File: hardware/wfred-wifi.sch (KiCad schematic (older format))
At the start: 9 parts, among them K401 UART_ESP, K402 UART_AVR, P401 ESP_BOOTLOAD, U401 ESP-12E

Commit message: Removed wiFred info from from clock project
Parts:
- removed K402: UART_AVR, Pin_Headers:Pin_Header_Straight_1x03_Pitch2.54mm, symbol CONN_3
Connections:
- net labels removed: THIS_RXD, THIS_TXD
- wire segments 29 -> 25
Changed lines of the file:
@@
 EESchema Schematic File Version 2
-LIBS:wfred_rev2-rescue
 LIBS:power
 LIBS:device
@@
 LIBS:my_devices
 LIBS:ESP8266
-LIBS:LDL1117S30R
-LIBS:MCP73831T-2ACI_OT
-LIBS:NCV8161BSN300T1G
-LIBS:wfred_rev2-cache
+LIBS:wfred_loconet_clock-cache
 EELAYER 25 0
 EELAYER END
 $Descr A4 11693 8268
 encoding utf-8
-Sheet 4 4
+Sheet 2 3
 Title "Wireless FREDI (and clock interface)"
 Date "2017-11-19"
@@
 Wire Wire Line
 	6750 2500 6700 2500
-Wire Wire Line
-	7700 2300 8050 2300
-Wire Wire Line
-	7700 2400 8050 2400
-Text GLabel 8050 2300 2    60   Output ~ 0
-THIS_RXD
-Text GLabel 8050 2400 2    60   Input ~ 0
-THIS_TXD
 $Comp
 L CONN_2 P401
@@
 Wire Wire Line
 	5200 2700 6750 2700
-$Comp
-L GND-RESCUE-wfred_rev2 #PWR041
-U 1 1 5A11FC27
-P 7850 2500
-F 0 "#PWR041" H 7850 2500 30  0001 C CNN
-F 1 "GND" H 7850 2430 30  0001 C CNN
-F 2 "" H 7850 2500 60  0001 C CNN
-F 3 "" H 7850 2500 60  0001 C CNN
-	1    7850 2500
-	1    0    0    -1
-$EndComp
 $Comp
 L R-RESCUE-wfred_rev2 R403
@@
 Wire Wire Line
 	5200 2900 6100 2900
-$Comp
-L CONN_3 K402
-U 1 1 5A11F053
-P 7350 2300
-F 0 "K402" V 7300 2300 50  0000 C CNN
-F 1 "UART_AVR" V 7400 2300 40  0000 C CNN
-F 2 "Pin_Headers:Pin_Header_Straight_1x03_Pitch2.54mm" H 7350 2300 60  0001 C CNN
-F 3 "" H 7350 2300 60  0001 C CNN
-F 4 "RND 205-00631" V 7350 2300 60  0001 C CNN "Reichelt"
-	1    7350 2300
-	-1   0    0    -1
-$EndComp
-Wire Wire Line
-	7700 2200 7850 2200
-Wire Wire Line
-	7850 2200 7850 2500
 Wire Wire Line
 	6100 2200 6100 2700

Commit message: Fix schematic after untangling from wiFred
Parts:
- C401, C402: symbol C-RESCUE-wfred_rev2 -> C
- R403, R404, R405: symbol R-RESCUE-wfred_rev2 -> R
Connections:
- net labels added: CLOCK1, CLOCK2, LOCO1, LOCO2, LOCO3, LOCO4
- wire segments 25 -> 31
- no-connect marks 14 -> 8
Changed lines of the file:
@@
 NoConn ~ 4550 3500
 $Comp
-L VCC #PWR038
+L VCC #PWR011
 U 1 1 5A11E004
 P 2700 1500
-F 0 "#PWR038" H 2700 1600 30  0001 C CNN
+F 0 "#PWR011" H 2700 1600 30  0001 C CNN
 F 1 "VCC" H 2700 1600 30  0000 C CNN
 F 2 "" H 2700 1500 60  0001 C CNN
@@
 Connection ~ 2700 2500
 $Comp
-L GND-RESCUE-wfred_rev2 #PWR039
+L GND #PWR012
 U 1 1 5A11E30D
 P 6700 3700
-F 0 "#PWR039" H 6700 3700 30  0001 C CNN
+F 0 "#PWR012" H 6700 3700 30  0001 C CNN
 F 1 "GND" H 6700 3630 30  0001 C CNN
 F 2 "" H 6700 3700 60  0001 C CNN
@@
 Connection ~ 6700 3000
 $Comp
-L VCC #PWR040
+L VCC #PWR013
 U 1 1 5A11E4AA
 P 6300 1550
-F 0 "#PWR040" H 6300 1650 30  0001 C CNN
+F 0 "#PWR013" H 6300 1650 30  0001 C CNN
 F 1 "VCC" H 6300 1650 30  0000 C CNN
 F 2 "" H 6300 1550 60  0001 C CNN
@@
 	5200 2700 6750 2700
 $Comp
-L R-RESCUE-wfred_rev2 R403
+L R R403
 U 1 1 5A11FF91
 P 6100 1950
@@
 $EndComp
 $Comp
-L R-RESCUE-wfred_rev2 R404
+L R R404
 U 1 1 5A11FFE4
 P 6100 3350
@@
 $EndComp
 $Comp
-L R-RESCUE-wfred_rev2 R405
+L R R405
 U 1 1 5A120047
 P 6300 1950
@@
 	6100 2900 6100 3100
 $Comp
-L GND-RESCUE-wfred_rev2 #PWR042
+L GND #PWR014
 U 1 1 5A120E87
 P 6100 3700
-F 0 "#PWR042" H 6100 3700 30  0001 C CNN
+F 0 "#PWR014" H 6100 3700 30  0001 C CNN
 F 1 "GND" H 6100 3630 30  0001 C CNN
 F 2 "" H 6100 3700 60  0001 C CNN
@@
 Connection ~ 6700 2900
 $Comp
-L C-RESCUE-wfred_rev2 C401
+L C C401
 U 1 1 5A127BCA
 P 1200 2400
@@
 $EndComp
 $Comp
-L VCC #PWR043
+L VCC #PWR015
 U 1 1 5A127C0E
 P 1200 1800
-F 0 "#PWR043" H 1200 1900 30  0001 C CNN
+F 0 "#PWR015" H 1200 1900 30  0001 C CNN
 F 1 "VCC" H 1200 1900 30  0000 C CNN
 F 2 "" H 1200 1800 60  0001 C CNN
@@
 	1200 1800 1200 2200
 $Comp
-L GND-RESCUE-wfred_rev2 #PWR044
+L GND #PWR016
 U 1 1 5A127CDB
 P 1200 2900
-F 0 "#PWR044" H 1200 2900 30  0001 C CNN
+F 0 "#PWR016" H 1200 2900 30  0001 C CNN
 F 1 "GND" H 1200 2830 30  0001 C CNN
 F 2 "" H 1200 2900 60  0001 C CNN
@@
 	1200 2600 1200 2900
 $Comp
-L C-RESCUE-wfred_rev2 C402
+L C C402
 U 1 1 5A199174
 P 1500 2400
@@
 	1500 2800 1200 2800
 Connection ~ 1200 2800
-NoConn ~ 5200 2500
-NoConn ~ 5200 2600
-NoConn ~ 3400 2600
-NoConn ~ 3400 2700
-NoConn ~ 3400 2800
-NoConn ~ 3400 2900
 NoConn ~ 3400 2400
 NoConn ~ 3400 2300
+Text GLabel 3200 2600 0    60   Input ~ 0
+LOCO1
+Wire Wire Line
+	3200 2600 3400 2600
+Text GLabel 3200 2700 0    60   Input ~ 0
+LOCO2
+Text GLabel 3200 2800 0    60   Input ~ 0
+LOCO3
+Text GLabel 3200 2900 0    60   Input ~ 0
+LOCO4
+Wire Wire Line
+	3200 2900 3400 2900
+Wire Wire Line
+	3400 2800 3200 2800
+Wire Wire Line
+	3200 2700 3400 2700
+Text GLabel 5500 2500 2    60   Output ~ 0
+CLOCK1
+Text GLabel 5500 2600 2    60   Output ~ 0
+CLOCK2
+Wire Wire Line
+	5200 2500 5500 2500
+Wire Wire Line
+	5500 2600 5200 2600
 $EndSCHEMATC

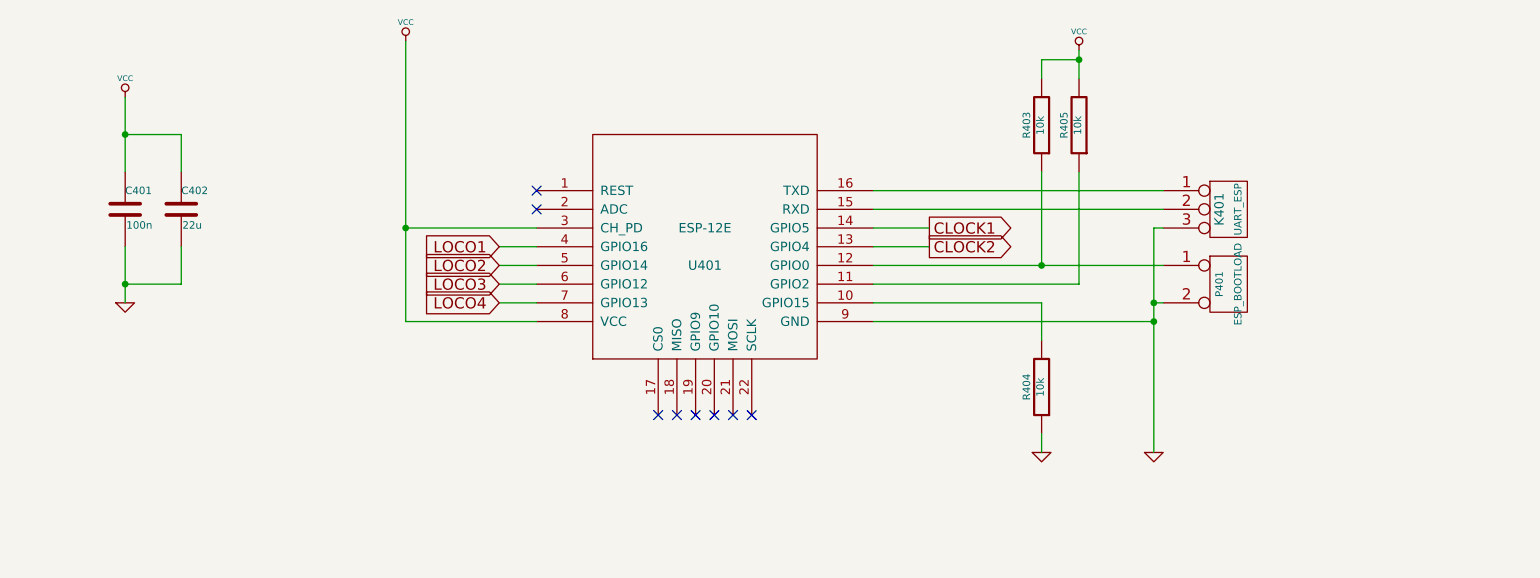
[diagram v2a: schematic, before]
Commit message: Change clock schematic and PCB
- Remove slide switches, replace with single push button
- Add status LED
- Re-add battery measurement connection

- Change PCB form factor to fit NewAgeEnclosures Compact AA housing
- Re-layout PCB
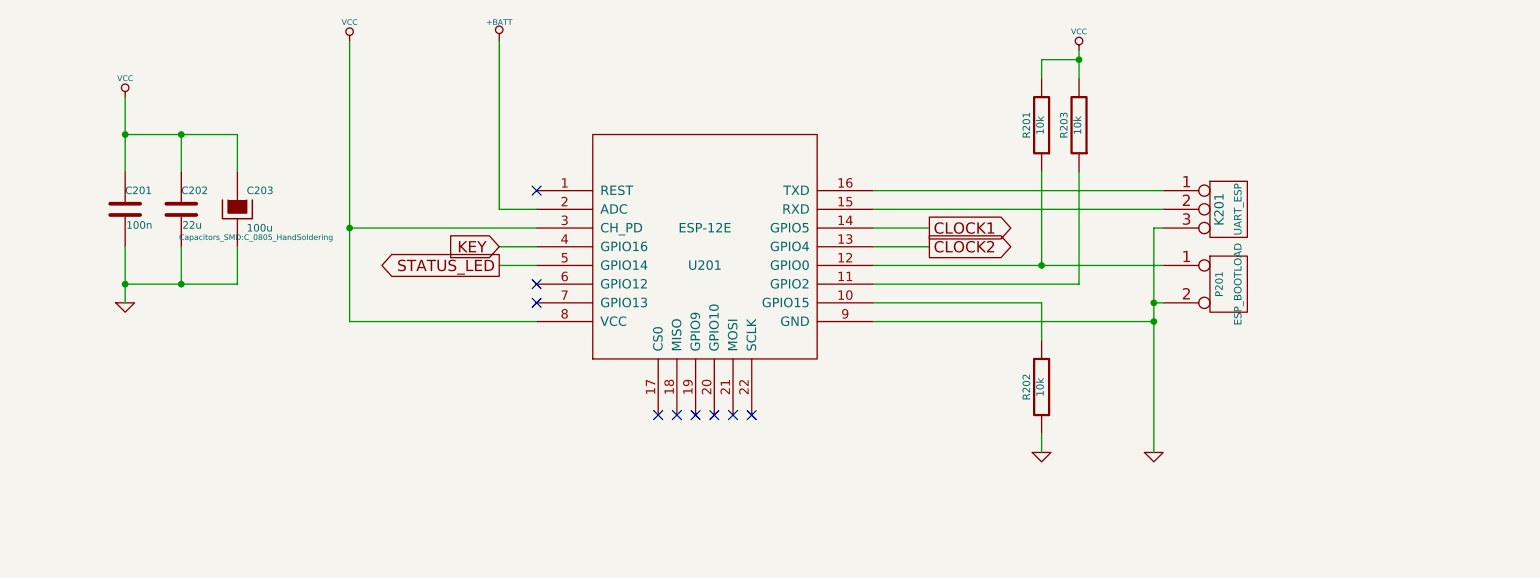
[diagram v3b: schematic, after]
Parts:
- added C203: 100u, Capacitors_SMD:C_0805_HandSoldering, symbol CAPAPOL
- renumbered C401 to C201, C402 to C202, K401 to K201, P401 to P201, R403 to R201, R404 to R202, R405 to R203, U401 to U201
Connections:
- net GND: now also C203.2
- net VCC: now also C203.1
- net +BATT: now reaches U201.2 (ADC)
- net LOCO1 renamed KEY
- net LOCO2 renamed STATUS_LED
- net LOCO3: no longer names the net of U201.6 (GPIO12)
- net LOCO4: no longer names the net of U201.7 (GPIO13)
- no-connect marks 8 -> 9
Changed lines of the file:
@@
 $EndDescr
 $Comp
-L ESP-12E U401
+L ESP-12E U201
 U 1 1 5A11AA62
 P 4300 2600
-F 0 "U401" H 4300 2500 50  0000 C CNN
+F 0 "U201" H 4300 2500 50  0000 C CNN
 F 1 "ESP-12E" H 4300 2700 50  0000 C CNN
 F 2 "ESP8266:ESP-12E_SMD" H 4300 2600 50  0001 C CNN
@@
 L VCC #PWR011
 U 1 1 5A11E004
-P 2700 1500
-F 0 "#PWR011" H 2700 1600 30  0001 C CNN
-F 1 "VCC" H 2700 1600 30  0000 C CNN
-F 2 "" H 2700 1500 60  0001 C CNN
-F 3 "" H 2700 1500 60  0001 C CNN
-	1    2700 1500
-	1    0    0    -1
-$EndComp
-Wire Wire Line
-	2700 1500 2700 3000
-Wire Wire Line
-	2700 3000 3400 3000
-Wire Wire Line
-	3400 2500 2700 2500
-Connection ~ 2700 2500
+P 2400 1500
+F 0 "#PWR011" H 2400 1600 30  0001 C CNN
+F 1 "VCC" H 2400 1600 30  0000 C CNN
+F 2 "" H 2400 1500 60  0001 C CNN
+F 3 "" H 2400 1500 60  0001 C CNN
+	1    2400 1500
+	1    0    0    -1
+$EndComp
+Wire Wire Line
+	2400 1500 2400 3000
+Wire Wire Line
+	2400 3000 3400 3000
+Wire Wire Line
+	3400 2500 2400 2500
+Connection ~ 2400 2500
 $Comp
 L GND #PWR012
@@
 	5200 2400 6750 2400
 $Comp
-L CONN_3 K401
+L CONN_3 K201
 U 1 1 5A11EE74
 P 7100 2400
-F 0 "K401" V 7050 2400 50  0000 C CNN
+F 0 "K201" V 7050 2400 50  0000 C CNN
 F 1 "UART_ESP" V 7150 2400 40  0000 C CNN
 F 2 "Pin_Headers:Pin_Header_Straight_1x03_Pitch2.54mm" H 7100 2400 60  0001 C CNN
@@
 	6750 2500 6700 2500
 $Comp
-L CONN_2 P401
+L CONN_2 P201
 U 1 1 5A11F720
 P 7100 2800
-F 0 "P401" V 7050 2800 40  0000 C CNN
+F 0 "P201" V 7050 2800 40  0000 C CNN
 F 1 "ESP_BOOTLOAD" V 7150 2800 40  0000 C CNN
 F 2 "Pin_Headers:Pin_Header_Straight_1x02_Pitch2.54mm" H 7100 2800 60  0001 C CNN
@@
 	5200 2700 6750 2700
 $Comp
-L R R403
+L R R201
 U 1 1 5A11FF91
 P 6100 1950
-F 0 "R403" V 6180 1950 40  0000 C CNN
+F 0 "R201" V 6180 1950 40  0000 C CNN
 F 1 "10k" V 6107 1951 40  0000 C CNN
 F 2 "Capacitors_SMD:C_0805_HandSoldering" V 6030 1950 30  0001 C CNN
@@
 $EndComp
 $Comp
-L R R404
+L R R202
 U 1 1 5A11FFE4
 P 6100 3350
-F 0 "R404" V 6180 3350 40  0000 C CNN
+F 0 "R202" V 6180 3350 40  0000 C CNN
 F 1 "10k" V 6107 3351 40  0000 C CNN
 F 2 "Capacitors_SMD:C_0805_HandSoldering" V 6030 3350 30  0001 C CNN
@@
 $EndComp
 $Comp
-L R R405
+L R R203
 U 1 1 5A120047
 P 6300 1950
-F 0 "R405" V 6380 1950 40  0000 C CNN
+F 0 "R203" V 6380 1950 40  0000 C CNN
 F 1 "10k" V 6307 1951 40  0000 C CNN
 F 2 "Capacitors_SMD:C_0805_HandSoldering" V 6230 1950 30  0001 C CNN
@@
 Connection ~ 6700 2900
 $Comp
-L C C401
+L C C201
 U 1 1 5A127BCA
 P 1200 2400
-AR Path="/5A127BCA" Ref="C401"  Part="1"
-AR Path="/5A122619/5A127BCA" Ref="C401"  Part="1"
-F 0 "C401" H 1200 2500 40  0000 L CNN
+F 0 "C201" H 1200 2500 40  0000 L CNN
 F 1 "100n" H 1206 2315 40  0000 L CNN
 F 2 "Capacitors_SMD:C_0805_HandSoldering" H 1238 2250 30  0001 C CNN
@@
 	1200 2600 1200 2900
 $Comp
-L C C402
+L C C202
 U 1 1 5A199174
 P 1500 2400
-AR Path="/5A199174" Ref="C402"  Part="1"
-AR Path="/5A122619/5A199174" Ref="C402"  Part="1"
-F 0 "C402" H 1500 2500 40  0000 L CNN
+F 0 "C202" H 1500 2500 40  0000 L CNN
 F 1 "22u" H 1506 2315 40  0000 L CNN
 F 2 "Capacitors_SMD:C_0805_HandSoldering" H 1538 2250 30  0001 C CNN
@@
 $EndComp
 Wire Wire Line
-	1200 2000 1500 2000
+	1200 2000 1800 2000
 Wire Wire Line
 	1500 2000 1500 2200
@@
 	1500 2600 1500 2800
 Wire Wire Line
-	1500 2800 1200 2800
+	1200 2800 1800 2800
 Connection ~ 1200 2800
-NoConn ~ 3400 2400
 NoConn ~ 3400 2300
-Text GLabel 3200 2600 0    60   Input ~ 0
-LOCO1
 Wire Wire Line
 	3200 2600 3400 2600
-Text GLabel 3200 2700 0    60   Input ~ 0
-LOCO2
-Text GLabel 3200 2800 0    60   Input ~ 0
-LOCO3
-Text GLabel 3200 2900 0    60   Input ~ 0
-LOCO4
-Wire Wire Line
-	3200 2900 3400 2900
-Wire Wire Line
-	3400 2800 3200 2800
+Text GLabel 3200 2700 0    60   Output ~ 0
+STATUS_LED
 Wire Wire Line
 	3200 2700 3400 2700
@@
 Wire Wire Line
 	5500 2600 5200 2600
+Text GLabel 3200 2600 0    60   Input ~ 0
+KEY
+NoConn ~ 3400 2800
+NoConn ~ 3400 2900
+$Comp
+L CAPAPOL C203
+U 1 1 5C82A7FA
+P 1800 2400
+F 0 "C203" H 1850 2500 40  0000 L CNN
+F 1 "100u" H 1850 2300 40  0000 L CNN
+F 2 "Capacitors_SMD:C_0805_HandSoldering" H 1900 2250 30  0000 C CNN
+F 3 "" H 1800 2400 300 0000 C CNN
+	1    1800 2400
+	1    0    0    -1
+$EndComp
+Wire Wire Line
+	1800 2000 1800 2200
+Connection ~ 1500 2000
+Wire Wire Line
+	1800 2800 1800 2600
+Connection ~ 1500 2800
+$Comp
+L +BATT #PWR017
+U 1 1 5C82B48A
+P 3200 1500
+F 0 "#PWR017" H 3200 1450 20  0001 C CNN
+F 1 "+BATT" H 3200 1600 30  0000 C CNN
+F 2 "" H 3200 1500 60  0001 C CNN
+F 3 "" H 3200 1500 60  0001 C CNN
+	1    3200 1500
+	1    0    0    -1
+$EndComp
+Wire Wire Line
+	3200 1500 3200 2400
+Wire Wire Line
+	3200 2400 3400 2400
 $EndSCHEMATC

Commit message: Changed PCB and code to closer match first PCB
- Add battery measurement resistors
- Move key, status LED and clock I/O-pins around to match first PCB
  (except for CLOCK1 which is on low power pin in first version)
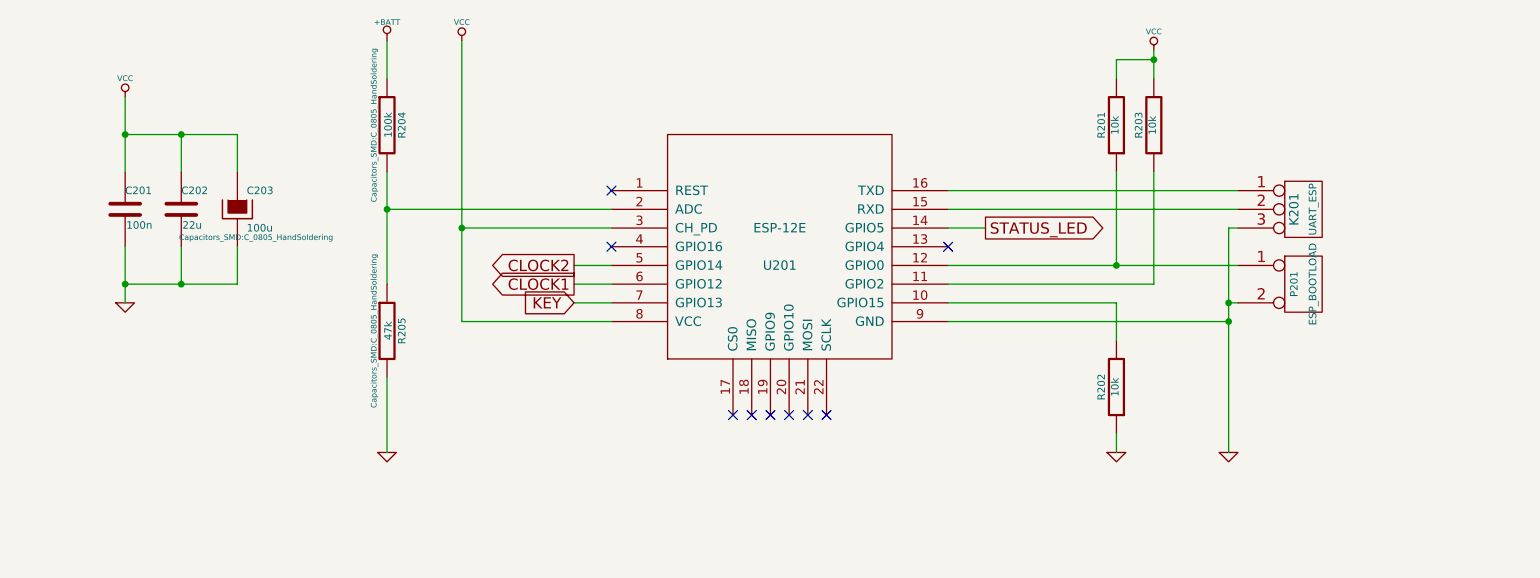
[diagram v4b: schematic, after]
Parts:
- added R204: 100k, Capacitors_SMD:C_0805_HandSoldering, symbol R
- added R205: 47k, Capacitors_SMD:C_0805_HandSoldering, symbol R
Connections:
- net +BATT: now also R204.1; no longer U201.2 (ADC)
- net CLOCK1: now also U201.6 (GPIO12); no longer U201.14 (GPIO5)
- net CLOCK2: now also U201.5 (GPIO14); no longer U201.13 (GPIO4)
- net GND: now also R205.2
- net KEY: now also U201.7 (GPIO13); no longer U201.4 (GPIO16)
- net STATUS_LED: now also U201.14 (GPIO5); no longer U201.5 (GPIO14)
- new net: R204.2, R205.1, U201.2 (ADC)
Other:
- moved on the sheet: K201, P201, R201, R202, R203, U201

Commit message: Added more keys to the PCB for adjusting the time
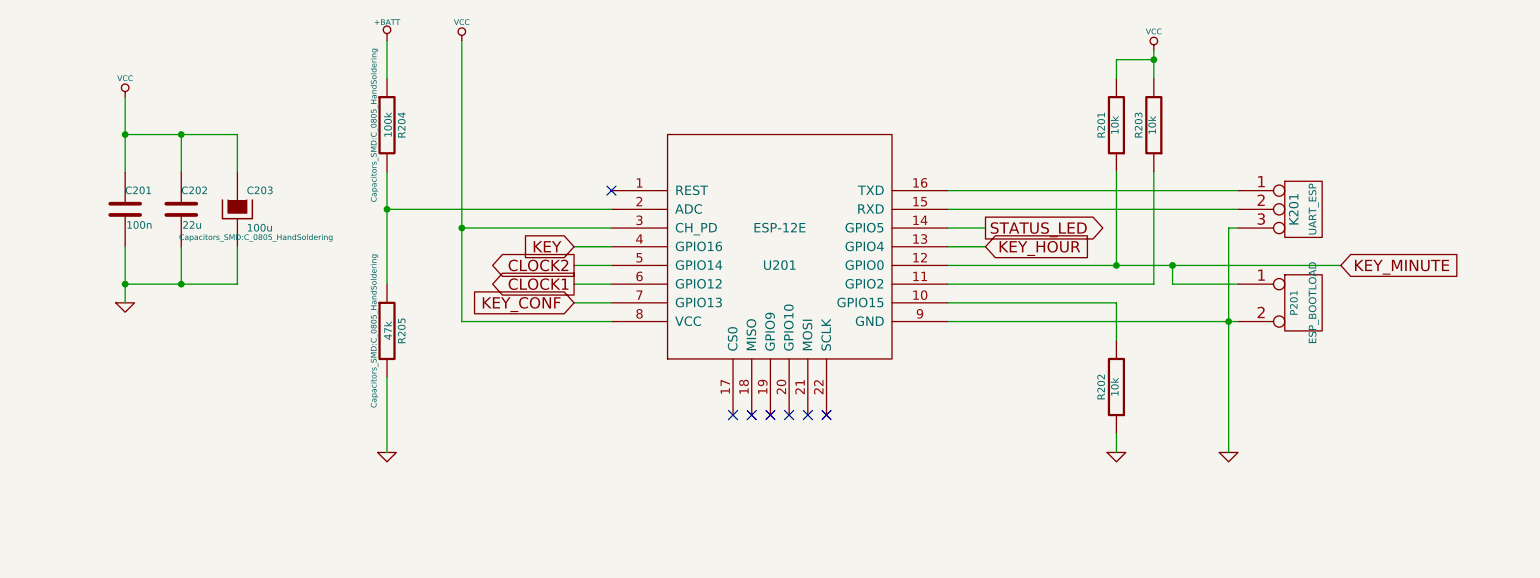
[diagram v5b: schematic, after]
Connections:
- net KEY: now also U201.4 (GPIO16); no longer U201.7 (GPIO13)
- net KEY_MINUTE: now reaches P201.1 (P1), R201.1, U201.12 (GPIO0)
- net KEY_HOUR: now reaches U201.13 (GPIO4)
- new net KEY_CONF: U201.7 (GPIO13)
- no-connect marks 9 -> 7
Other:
- moved on the sheet: P201
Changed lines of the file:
@@
 	7100 2500 7100 3700
 Wire Wire Line
-	7100 3000 5600 3000
+	5600 3000 7150 3000
 Connection ~ 7100 3000
 $Comp
@@
 L CONN_2 P201
 U 1 1 5A11F720
-P 7500 2800
-F 0 "P201" V 7450 2800 40  0000 C CNN
-F 1 "ESP_BOOTLOAD" V 7550 2800 40  0000 C CNN
-F 2 "Pin_Headers:Pin_Header_Straight_1x02_Pitch2.54mm" H 7500 2800 60  0001 C CNN
-F 3 "" H 7500 2800 60  0001 C CNN
-F 4 "RND 205-00631" V 7500 2800 60  0001 C CNN "Reichelt"
-	1    7500 2800
-	1    0    0    -1
-$EndComp
-Wire Wire Line
-	5600 2700 7150 2700
+P 7500 2900
+F 0 "P201" V 7450 2900 40  0000 C CNN
+F 1 "ESP_BOOTLOAD" V 7550 2900 40  0000 C CNN
+F 2 "Pin_Headers:Pin_Header_Straight_1x02_Pitch2.54mm" H 7500 2900 60  0001 C CNN
+F 3 "" H 7500 2900 60  0001 C CNN
+F 4 "RND 205-00631" V 7500 2900 60  0001 C CNN "Reichelt"
+	1    7500 2900
+	1    0    0    -1
+$EndComp
+Wire Wire Line
+	5600 2700 7700 2700
 $Comp
 L R R201
@@
 	5600 2900 6500 2900
 Wire Wire Line
-	6500 2200 6500 2700
+	6500 2700 6500 2200
 Connection ~ 6500 2700
 Wire Wire Line
@@
 Wire Wire Line
 	6500 1600 6700 1600
-Wire Wire Line
-	7150 2900 7100 2900
-Connection ~ 7100 2900
 $Comp
 L C C201
@@
 CLOCK2
 Text GLabel 3600 2900 0    60   Input ~ 0
-KEY
+KEY_CONF
 $Comp
 L CAPAPOL C203
@@
 Wire Wire Line
 	5600 2500 5800 2500
-NoConn ~ 5600 2600
 $Comp
 L GND #PWR018
@@
 Wire Wire Line
 	2600 3300 2600 3700
-NoConn ~ 3800 2600
 Wire Wire Line
 	3800 2800 3600 2800
+Text GLabel 3600 2600 0    60   Input ~ 0
+KEY
+Wire Wire Line
+	3600 2600 3800 2600
+Text GLabel 5800 2600 2    60   Input ~ 0
+KEY_HOUR
+Text GLabel 7700 2700 2    60   Input ~ 0
+KEY_MINUTE
+Wire Wire Line
+	7150 2800 6800 2800
+Wire Wire Line
+	6800 2800 6800 2700
+Connection ~ 6800 2700
+Wire Wire Line
+	5800 2600 5600 2600
 $EndSCHEMATC
